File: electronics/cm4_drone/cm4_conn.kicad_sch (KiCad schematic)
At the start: 5 parts, among them U5 Compute_Module_4_Connectors

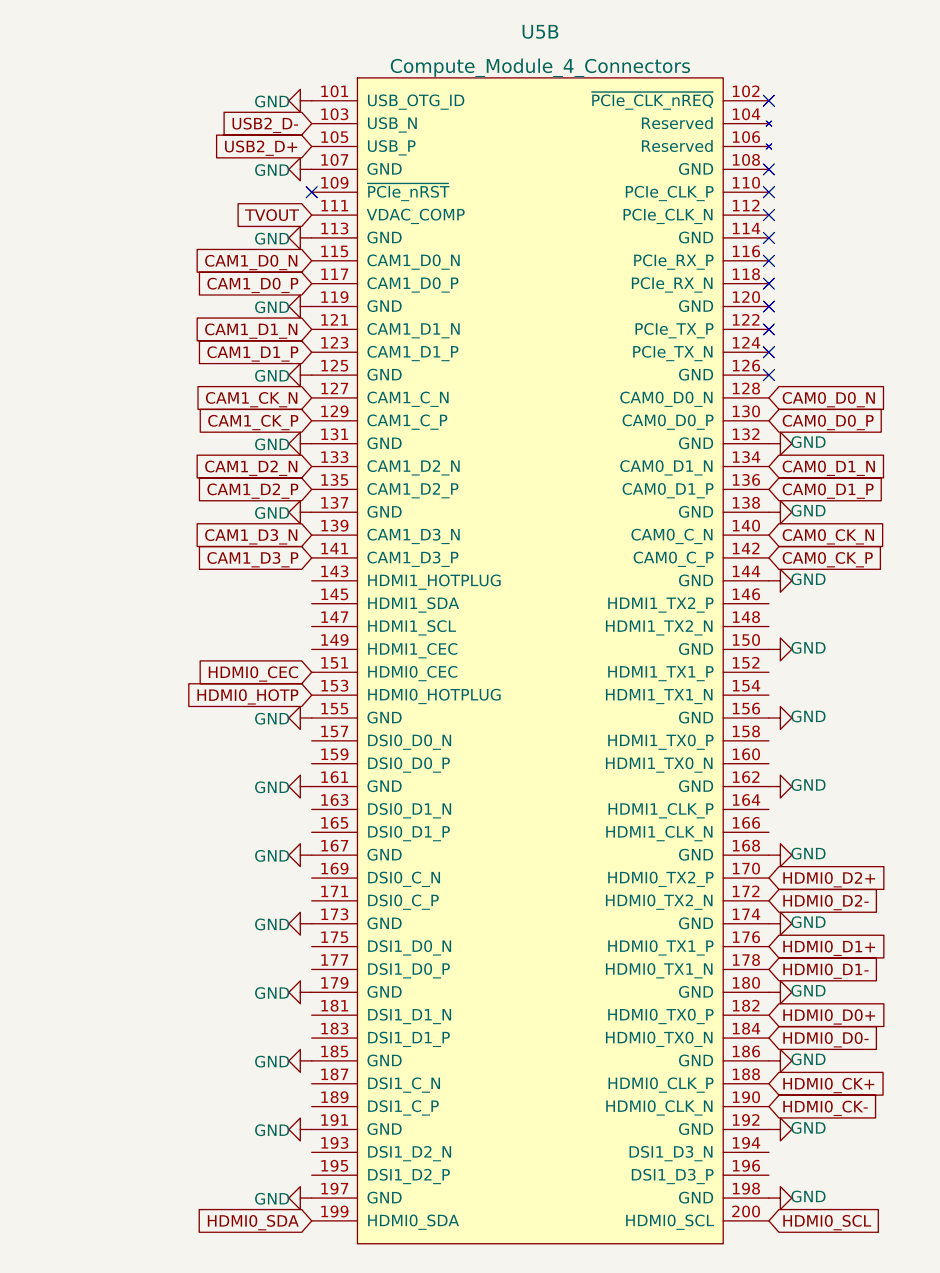
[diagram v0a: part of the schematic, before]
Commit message: wip new pcb with m2 connector
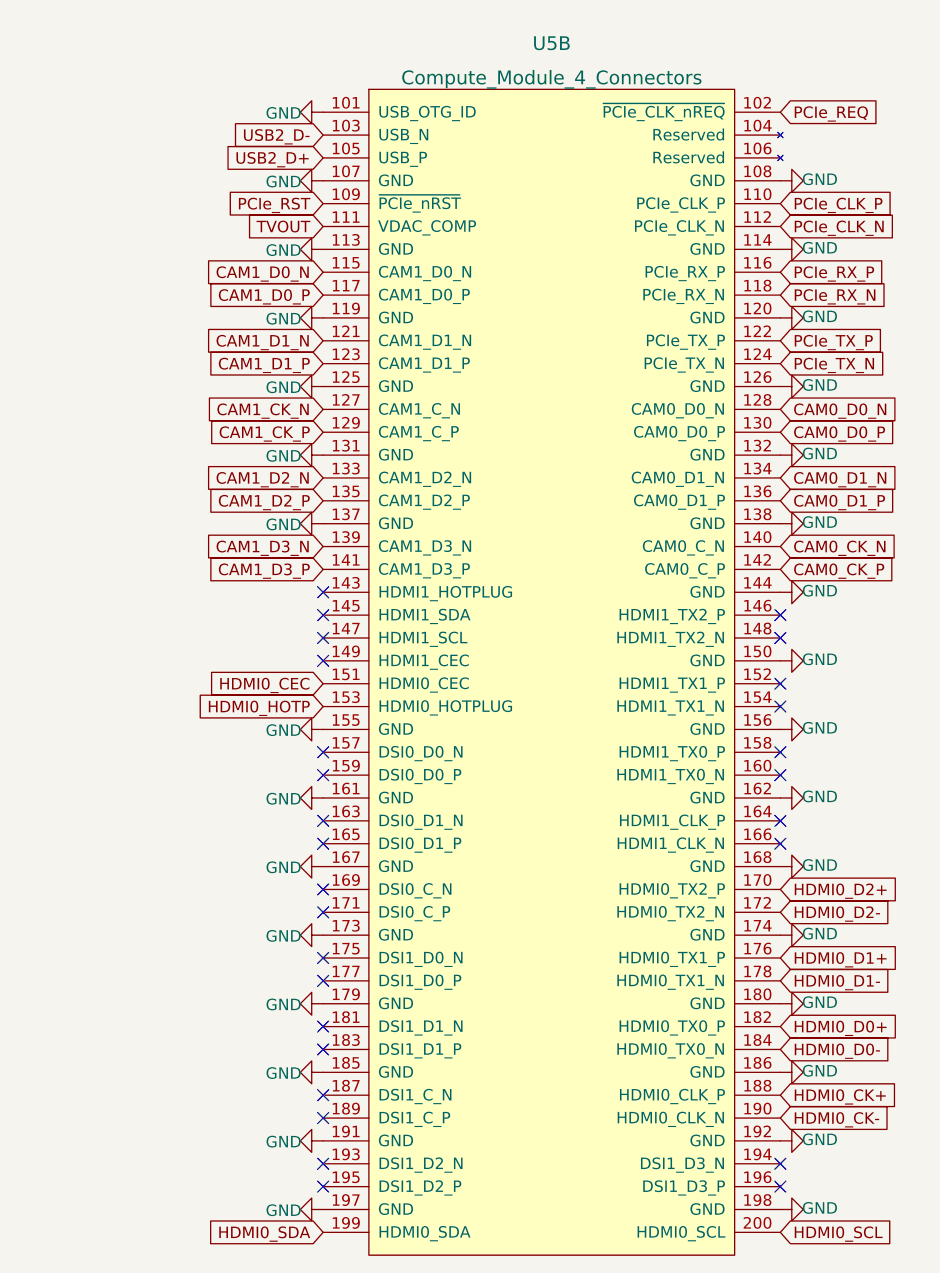
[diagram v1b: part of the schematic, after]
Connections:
- net GND: now also U5.108 (GND), U5.114 (GND), U5.120 (GND), U5.126 (GND)
- net PCIe_REQ: now reaches U5.102 (~{PCIe_CLK_nREQ})
- net PCIe_RST: now reaches U5.109 (~{PCIe_nRST})
- net PCIe_CLK_P: now reaches U5.110 (PCIe_CLK_P)
- net PCIe_CLK_N: now reaches U5.112 (PCIe_CLK_N)
- net PCIe_RX_P: now reaches U5.116 (PCIe_RX_P)
- net PCIe_RX_N: now reaches U5.118 (PCIe_RX_N)
- net PCIe_TX_P: now reaches U5.122 (PCIe_TX_P)
- net PCIe_TX_N: now reaches U5.124 (PCIe_TX_N)
- no-connect marks 38 -> 54
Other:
- moved on the sheet: U5B
